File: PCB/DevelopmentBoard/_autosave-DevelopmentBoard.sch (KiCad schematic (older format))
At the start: 27 parts, among them J2 Conn_01x04_MountingPin-Payloa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, J5 Conn_01x04_MountingPin, U1 D24V22F5_VoltageRegulator, U2 Barometer_Grove, U3 RASPBERRY_PI_3_MODEL_B+, U4 Conn_01x08_DevBoardSymbols, U6 MCP3008_ADC, U7 Conn_01x06_DevBoard_Symbols, X1 XT30, X2 XT30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

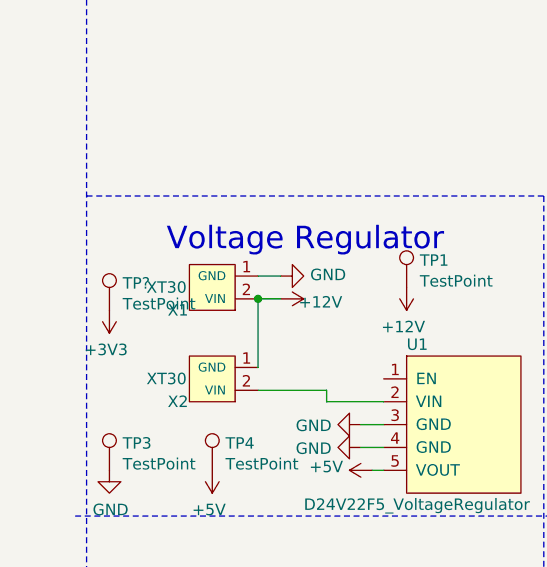
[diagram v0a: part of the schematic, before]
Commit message: Added 3.3V testpoint
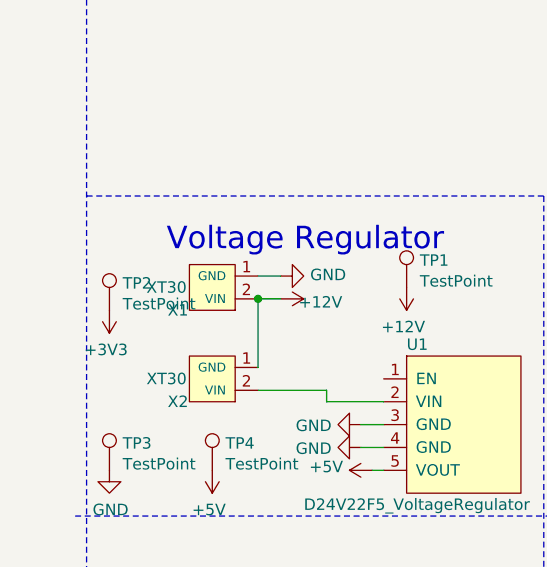
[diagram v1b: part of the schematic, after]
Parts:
- gave numbers to parts that had none: 1
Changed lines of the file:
@@
 $EndComp
 $Comp
-L Connector:TestPoint TP?
+L Connector:TestPoint TP2
 U 1 1 623429F1
 P 1100 15350
-F 0 "TP?" H 1158 15468 50  0000 L CNN
+F 0 "TP2" H 1158 15468 50  0000 L CNN
 F 1 "TestPoint" H 1158 15377 50  0000 L CNN
 F 2 "TestPoint:TestPoint_Pad_D2.5mm" H 1300 15350 50  0001 C CNN
@@
 $EndComp
 $Comp
-L power:+3V3 #PWR?
+L power:+3V3 #PWR0120
 U 1 1 623433B8
 P 1100 15350
-F 0 "#PWR?" H 1100 15200 50  0001 C CNN
+F 0 "#PWR0120" H 1100 15200 50  0001 C CNN
 F 1 "+3V3" H 1115 15523 50  0000 C CNN
 F 2 "" H 1100 15350 50  0001 C CNN
